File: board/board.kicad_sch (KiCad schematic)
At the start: 17 parts, among them J1 UART, J2 008_USB, J3 DebugEdge_02x05, J4 019_100BASE-T_with_CT, J5 ADC_2x3, J7 SPI_2x3, J8 I2C_2x2, J9 UART_2x2

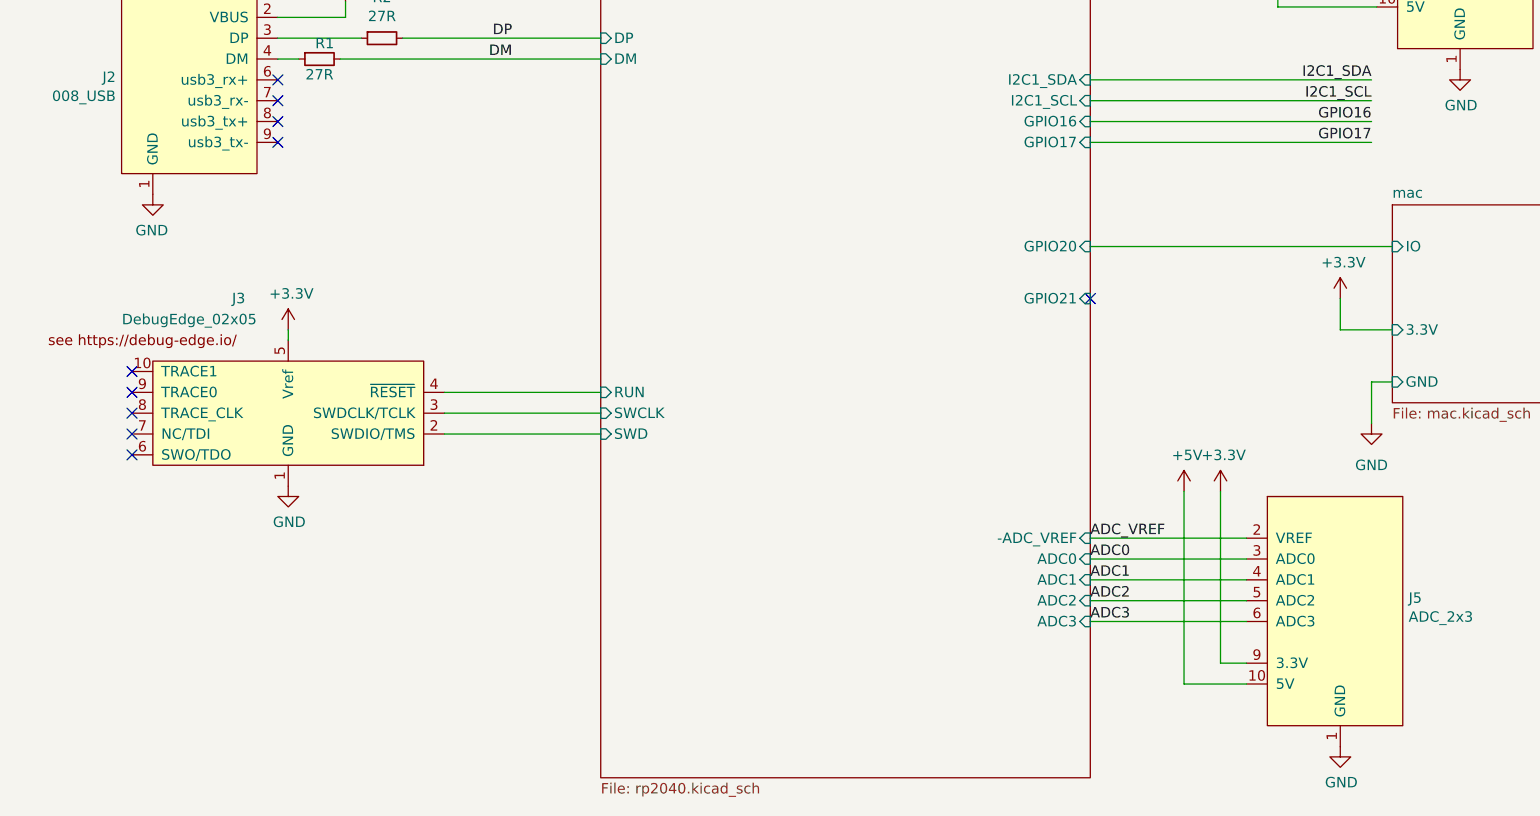
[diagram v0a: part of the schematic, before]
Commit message: added needle addapter
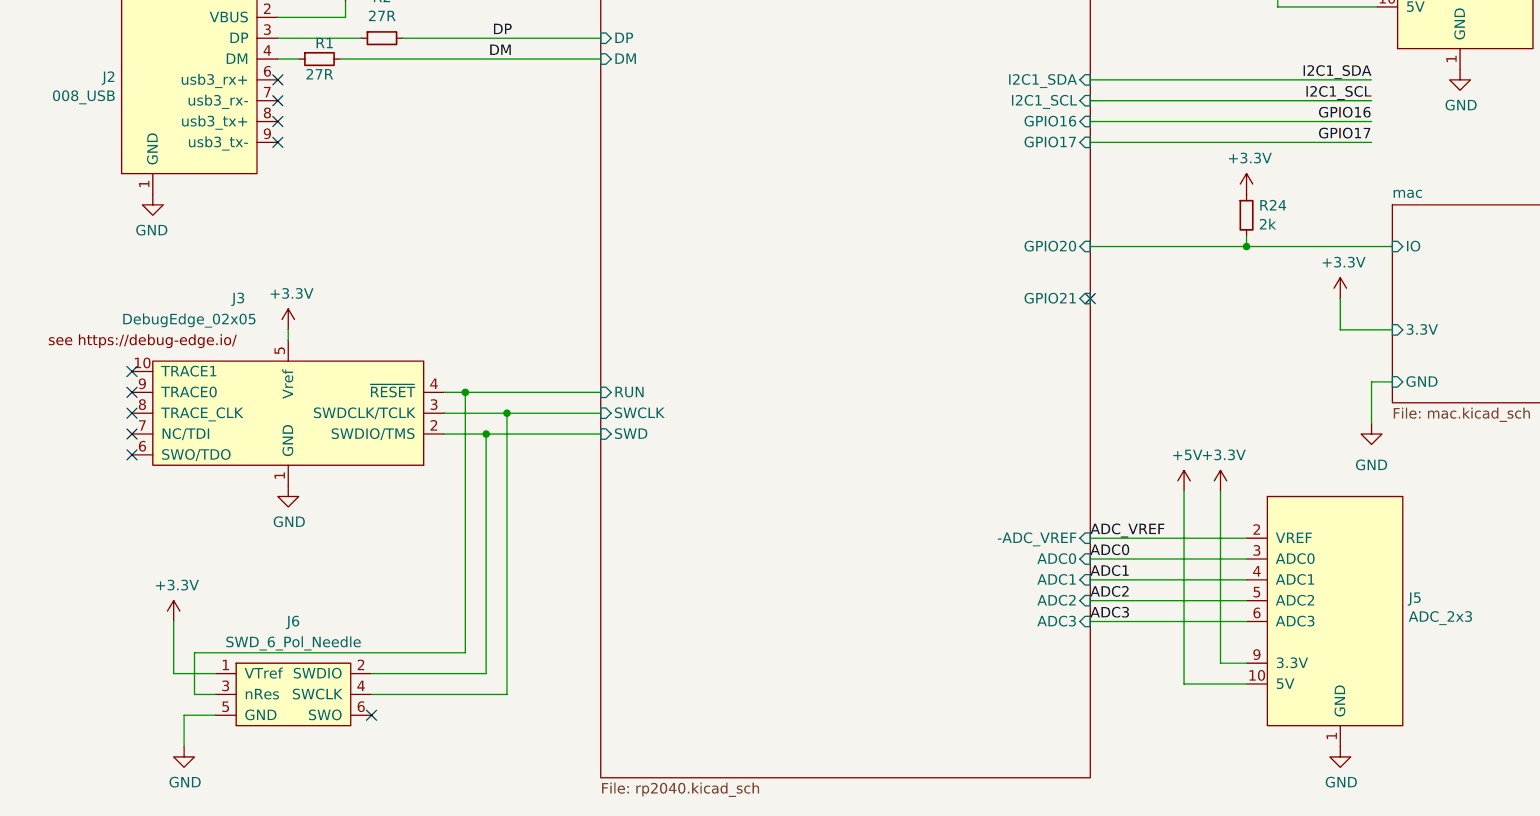
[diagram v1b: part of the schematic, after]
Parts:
- added J6: SWD_6_Pol_Needle, c001:SWD6pol, symbol c001:SWD_6_Pol_Needle
- added R24: 2k, Resistor_SMD:R_0603_1608Metric, symbol Device:R_Small
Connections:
- net +3V3: now also J6.1 (VTref), R24.1
- net GND: now also J6.5 (GND)
- net mac/IO: now also R24.2
- net rp2040/RUN: now also J6.3 (nRes)
- net rp2040/SWCLK: now also J6.4 (SWCLK)
- net rp2040/SWD: now also J6.2 (SWDIO)
- no-connect marks 11 -> 12

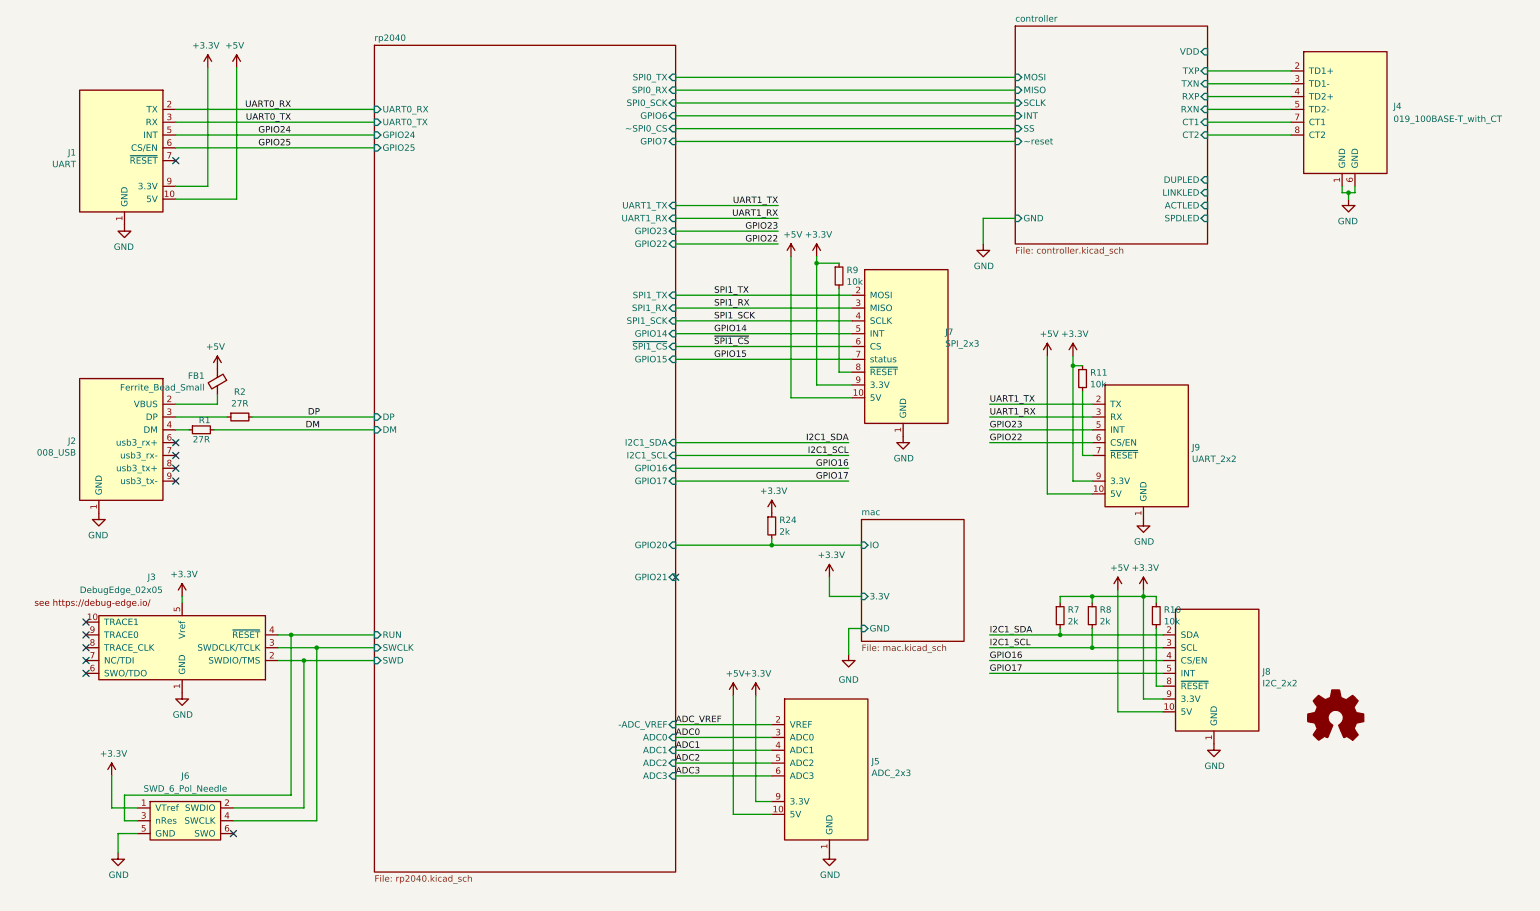
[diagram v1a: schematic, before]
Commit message: improved power integrity
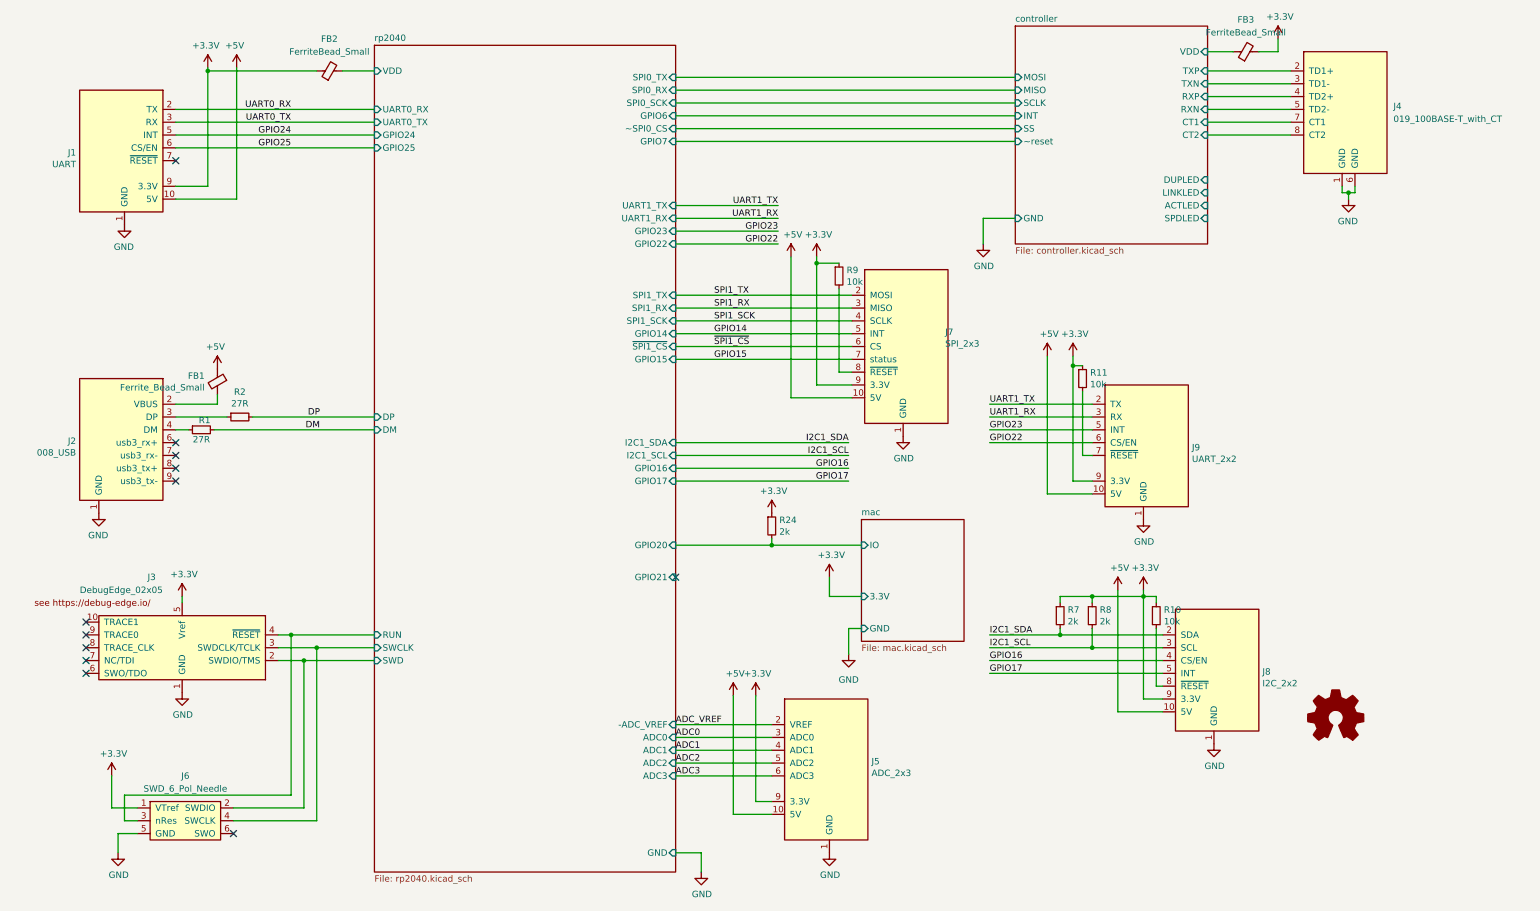
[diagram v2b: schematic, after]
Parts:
- added FB2, FB3: FerriteBead_Small, Inductor_SMD:L_0603_1608Metric, symbol Device:FerriteBead_Small
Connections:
- net +3V3: now also FB2.1, FB3.2
- net controller/VDD: now also FB3.1
- new net rp2040/VDD: FB2.2
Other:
- sheet rp2040 ports: added GND, VDD; removed none

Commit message: updated put_on_edge connectors
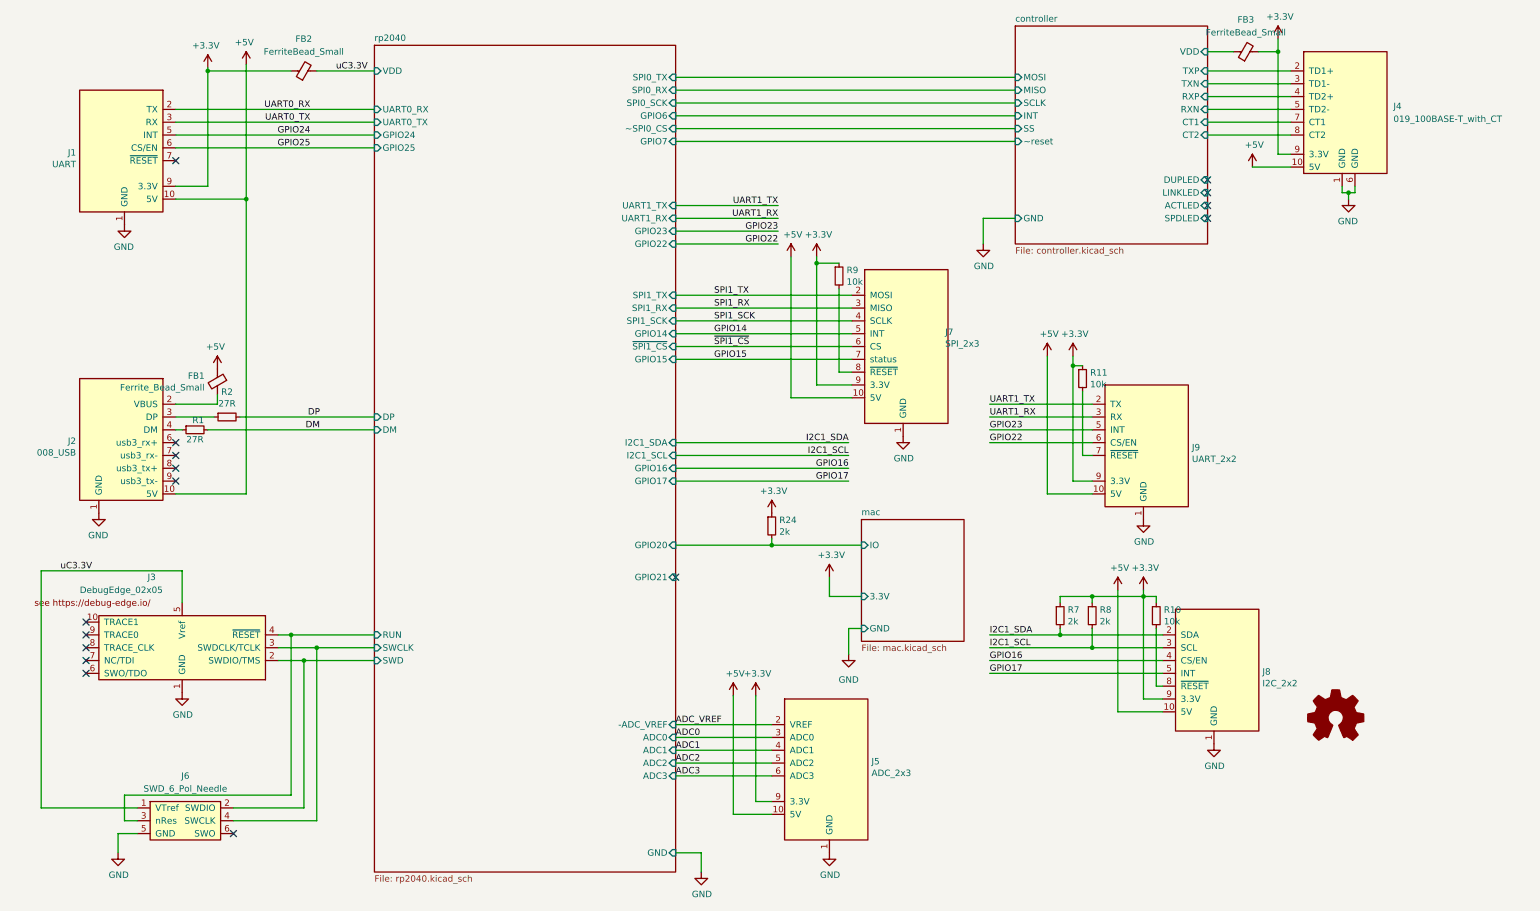
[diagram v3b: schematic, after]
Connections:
- net +5V: now also J2.10 (5V), J4.10 (5V)
- net +3V3 renamed +3.3V
- net +3.3V: now also J4.9 (3.3V); no longer J3.5 (Vref), J6.1 (VTref)
- net rp2040/VDD renamed uC3.3V
- net uC3.3V: now also J3.5 (Vref), J6.1 (VTref)
- no-connect marks 12 -> 16
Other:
- moved on the sheet: FB2, R1, R2

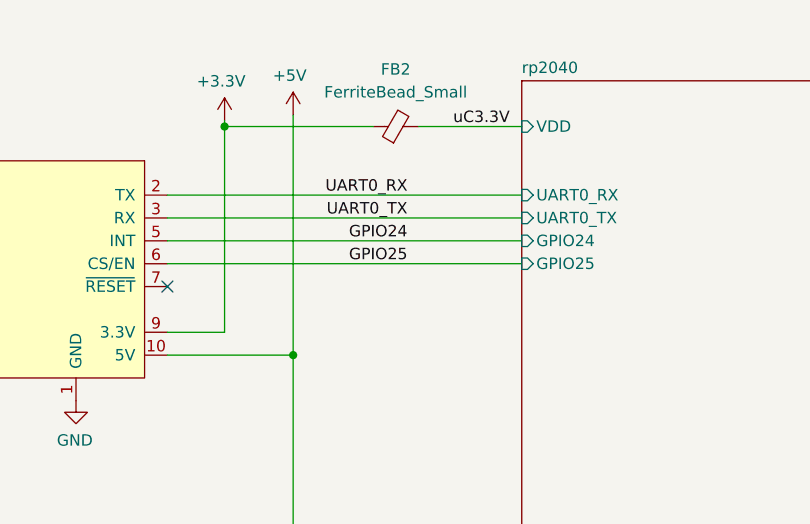
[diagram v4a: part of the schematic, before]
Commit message: added boot select button and standard (small) flash
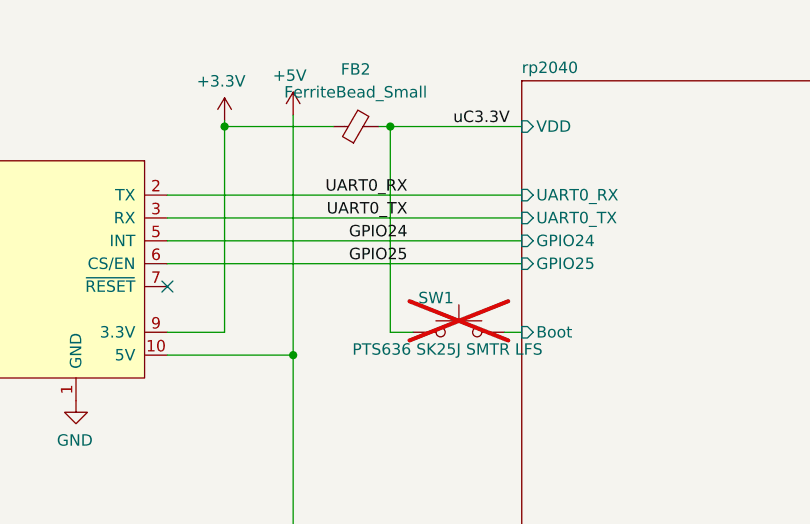
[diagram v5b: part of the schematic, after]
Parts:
- added SW1: PTS636 SK25J SMTR LFS, Resistor_SMD:R_2512_6332Metric, symbol Switch:SW_Push
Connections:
- net uC3.3V: now also SW1.1
- new net rp2040/Boot: SW1.2
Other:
- sheet rp2040 ports: added Boot; removed none
- moved on the sheet: FB2
